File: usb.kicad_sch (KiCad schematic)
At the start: 4 parts, among them J1 USB_C_Receptacle_USB2.0_16P

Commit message: Updated Footprints
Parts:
- C27: footprint (none) -> Capacitor_SMD:C_0603_1608Metric_Pad1.08x0.95mm_HandSolder
- J1: footprint (none) -> Connector_USB:USB_C_Receptacle_GCT_USB4105-xx-A_16P_TopMnt_Horizontal
- R7, R8: footprint (none) -> Resistor_SMD:R_0402_1005Metric
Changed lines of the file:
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@@
 			)
 		)
-		(property "Footprint" ""
+		(property "Footprint" "Capacitor_SMD:C_0603_1608Metric_Pad1.08x0.95mm_HandSolder"
 			(at 127.3048 123.19 0)
 			(effects
@@
 			)
 		)
-		(property "Footprint" ""
+		(property "Footprint" "Resistor_SMD:R_0402_1005Metric"
 			(at 172.72 86.868 90)
 			(effects
@@
 			)
 		)
-		(property "Footprint" ""
+		(property "Footprint" "Resistor_SMD:R_0402_1005Metric"
 			(at 172.72 84.328 90)
 			(effects
@@
 			)
 		)
-		(property "Footprint" ""
+		(property "Footprint" "Connector_USB:USB_C_Receptacle_GCT_USB4105-xx-A_16P_TopMnt_Horizontal"
 			(at 139.7 92.71 0)
 			(effects

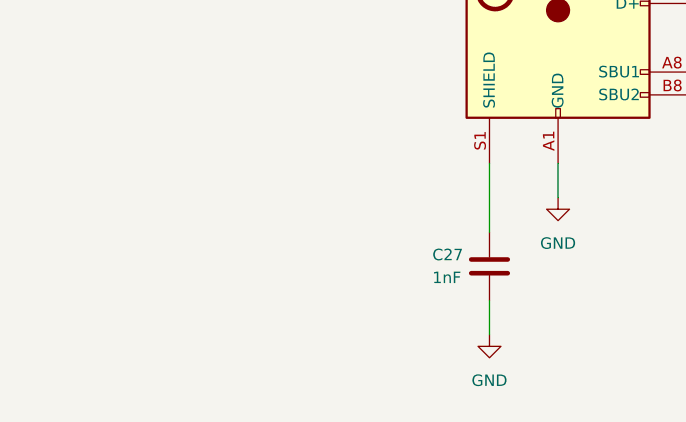
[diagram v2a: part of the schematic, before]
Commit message: Added test Antenna
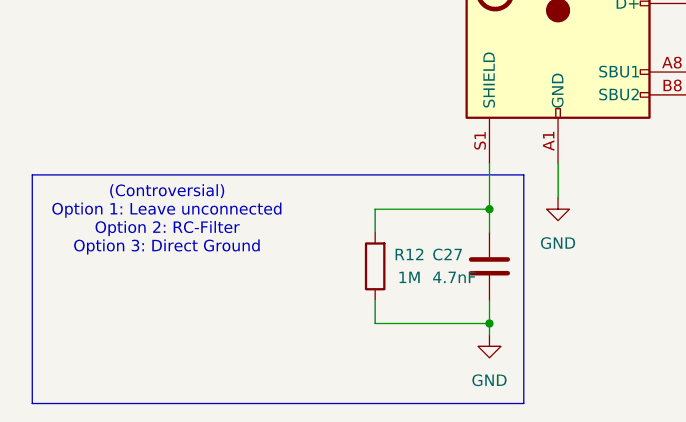
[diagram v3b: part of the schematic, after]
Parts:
- added R12: 1M, Resistor_SMD:R_0402_1005Metric, symbol Device:R
- C27: value 1nF -> 4.7nF
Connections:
- net GND: now also R12.1
- net at C27.2, J1.S1 (SHIELD): now also R12.2
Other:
- note added: "(Controversial) Option 1: Leave unconnected Option 2: RC-Filter Option 3: Direct Ground"
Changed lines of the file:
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@@
 	(generator_version "9.0")
 	(paper "A4")
+	(rectangle
+		(start 77.47 116.84)
+		(end 132.08 142.24)
+		(stroke
+			(width 0)
+			(type default)
+		)
+		(fill
+			(type none)
+		)
+	)
+	(text "(Controversial)\nOption 1: Leave unconnected\nOption 2: RC-Filter\nOption 3: Direct Ground"
+		(exclude_from_sim no)
+		(at 92.456 121.92 0)
+		(effects
+			(font
+				(size 1.27 1.27)
+			)
+		)
+	)
+	(junction
+		(at 128.27 120.65)
+		(diameter 0)
+		(color 0 0 0 0)
+	)
 	(junction
 		(at 180.34 83.82)
@@
 	)
 	(junction
+		(at 128.27 133.35)
+		(diameter 0)
+		(color 0 0 0 0)
+	)
+	(junction
 		(at 154.94 96.52)
 		(diameter 0)
@@
 	(wire
 		(pts
-			(xy 128.27 130.81) (xy 128.27 134.62)
+			(xy 128.27 130.81) (xy 128.27 133.35)
 		)
 		(stroke
@@
 	(wire
 		(pts
+			(xy 115.57 123.19) (xy 115.57 120.65)
+		)
+		(stroke
+			(width 0)
+			(type default)
+		)
+	)
+	(wire
+		(pts
 			(xy 135.89 115.57) (xy 135.89 119.38)
 		)
@@
 	(wire
 		(pts
+			(xy 115.57 120.65) (xy 128.27 120.65)
+		)
+		(stroke
+			(width 0)
+			(type default)
+		)
+	)
+	(wire
+		(pts
+			(xy 128.27 133.35) (xy 128.27 134.62)
+		)
+		(stroke
+			(width 0)
+			(type default)
+		)
+	)
+	(wire
+		(pts
+			(xy 115.57 133.35) (xy 128.27 133.35)
+		)
+		(stroke
+			(width 0)
+			(type default)
+		)
+	)
+	(wire
+		(pts
 			(xy 154.94 92.71) (xy 154.94 91.44)
 		)
@@
 	(wire
 		(pts
-			(xy 128.27 115.57) (xy 128.27 123.19)
+			(xy 115.57 130.81) (xy 115.57 133.35)
+		)
+		(stroke
+			(width 0)
+			(type default)
+		)
+	)
+	(wire
+		(pts
+			(xy 128.27 115.57) (xy 128.27 120.65)
 		)
 		(stroke
@@
 		(pts
 			(xy 180.34 83.82) (xy 180.34 82.55)
+		)
+		(stroke
+			(width 0)
+			(type default)
+		)
+	)
+	(wire
+		(pts
+			(xy 128.27 120.65) (xy 128.27 123.19)
 		)
 		(stroke
@@
 				(justify left)
 				(hide yes)
+			)
+		)
+	)
+	(symbol
+		(lib_id "Device:R")
+		(at 115.57 127 180)
+		(unit 1)
+		(exclude_from_sim no)
+		(in_bom yes)
+		(on_board yes)
+		(dnp no)
+		(property "Reference" "R12"
+			(at 119.38 125.73 0)
+			(effects
+				(font
+					(size 1.27 1.27)
+				)
+			)
+		)
+		(property "Value" "1M"
+			(at 119.38 128.27 0)
+			(effects
+				(font
+					(size 1.27 1.27)
+				)
+			)
+		)
+		(property "Footprint" "Resistor_SMD:R_0402_1005Metric"
+			(at 117.348 127 90)
+			(effects
+				(font
+					(size 1.27 1.27)
+				)
+				(hide yes)
+			)
+		)
+		(property "Datasheet" "~"
+			(at 115.57 127 0)
+			(effects
+				(font
+					(size 1.27 1.27)
+				)
+				(hide yes)
+			)
+		)
+		(property "Description" "Resistor"
+			(at 115.57 127 0)
+			(effects
+				(font
+					(size 1.27 1.27)
+				)
+				(hide yes)
+			)
+		)
+		(pin "1"
+		)
+		(pin "2"
+		)
+		(instances
+			(project "Slim Keyboard"
+				(path "/5d65a0d4-45a3-4af0-996a-c0381d04499a/f42a8a8a-4a34-440a-8e58-9c442fe0d23e/16a43eb5-0990-4f5c-a71d-12a9055d92a0"
+					(reference "R12")
+					(unit 1)
+				)
 			)
 		)
@@
 			)
 		)
-		(property "Value" "1nF"
+		(property "Value" "4.7nF"
 			(at 121.92 128.27 0)
 			(effects

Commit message: Added actual JST connector
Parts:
- C27: footprint Capacitor_SMD:C_0603_1608Metric_Pad1.08x0.95mm_HandSolder -> Capacitor_SMD:C_0402_1005Metric
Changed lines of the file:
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@@
 			)
 		)
-		(property "Footprint" "Capacitor_SMD:C_0603_1608Metric_Pad1.08x0.95mm_HandSolder"
+		(property "Footprint" "Capacitor_SMD:C_0402_1005Metric"
 			(at 127.3048 123.19 0)
 			(effects

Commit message: Started PCB design
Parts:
- C27, R12: now not fitted
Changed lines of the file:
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@@
 		(in_bom yes)
 		(on_board yes)
-		(dnp no)
+		(dnp yes)
 		(property "Reference" "R12"
 			(at 119.38 125.73 0)
@@
 		(in_bom yes)
 		(on_board yes)
-		(dnp no)
+		(dnp yes)
 		(property "Reference" "C27"
 			(at 121.92 125.73 0)
